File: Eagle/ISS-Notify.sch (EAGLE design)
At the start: 54 parts, among them J1 AVRISP, J2 JST2, J3 PROTOSPACE2, SW1 9077-1, SW2 SWITCH, U1 ATMEGA32U4, U2 MCP7940N, U3 TPS63001, U4 MCP73811, U5 TLC5971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

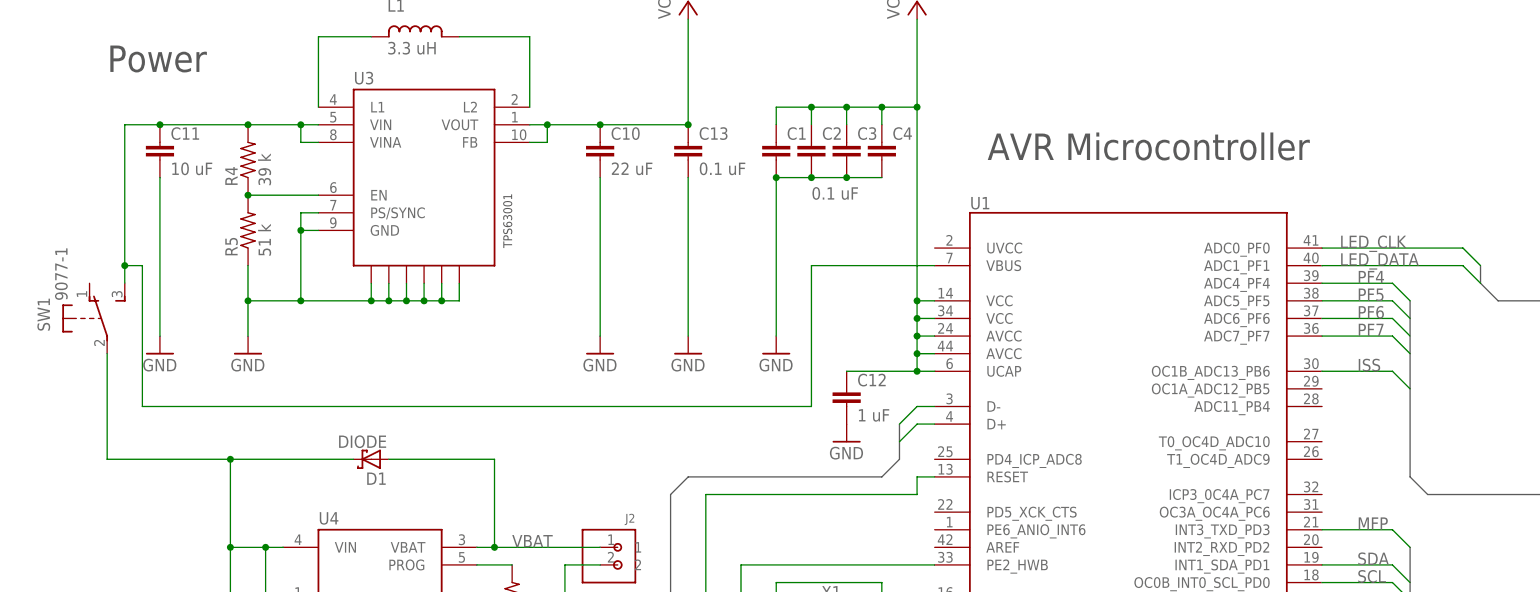
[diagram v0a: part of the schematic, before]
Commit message: bat sense signal
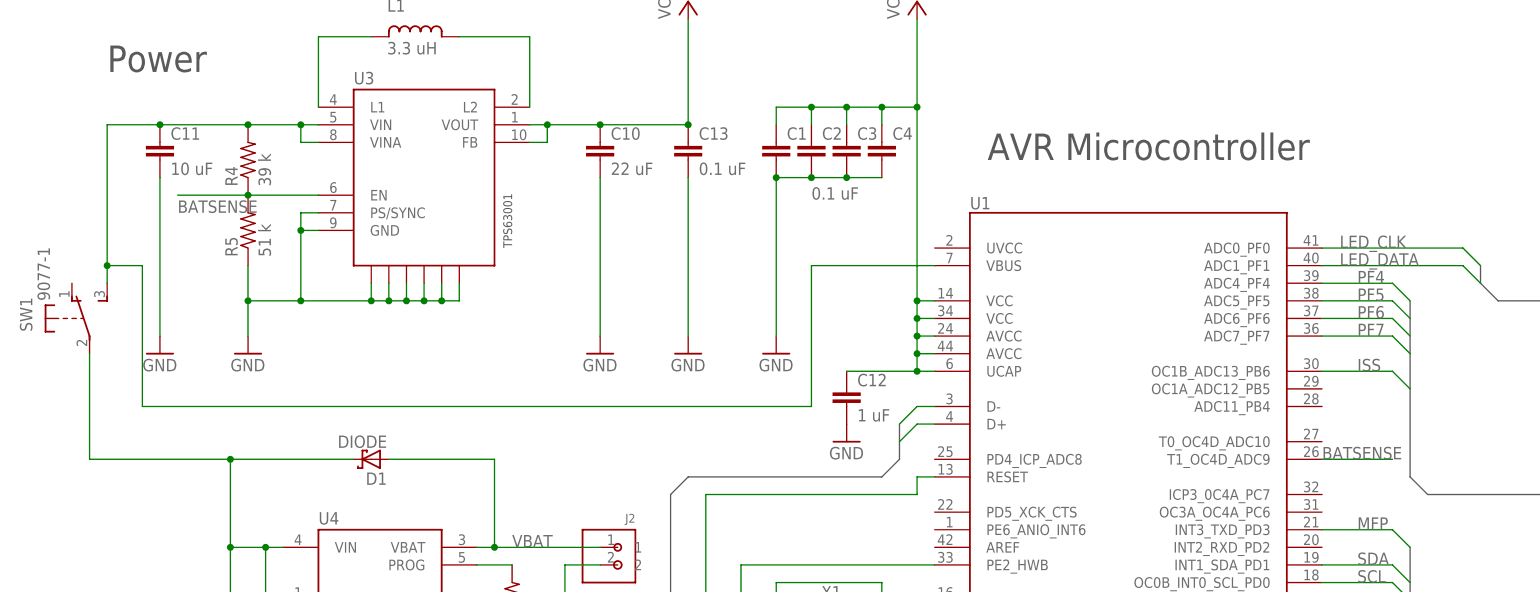
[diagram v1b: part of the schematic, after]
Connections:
- removed net N$3: R4.1, R5.2, U3.EN
- new net BATSENSE: R4.1, R5.2, U1.T1_OC4D_ADC9, U3.EN
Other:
- moved on the sheet: SW1
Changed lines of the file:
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@@
 <attribute name="VALUE" x="137.922" y="159.258" size="1.778" layer="96" rot="R180"/>
 </instance>
-<instance part="SW1" gate="1" x="30.48" y="205.74"/>
+<instance part="SW1" gate="1" x="27.94" y="205.74"/>
 <instance part="U4" gate="G$1" x="68.58" y="167.64"/>
 <instance part="R6" gate="R" x="88.9" y="165.1" rot="R90"/>
@@
 </segment>
 </net>
-<net name="N$3" class="0">
-<segment>
-<pinref part="R4" gate="R" pin="1"/>
-<pinref part="R5" gate="R" pin="2"/>
-<pinref part="U3" gate="G$1" pin="EN"/>
-<wire x1="60.96" y1="223.52" x2="50.8" y2="223.52" width="0.1524" layer="91"/>
-<junction x="50.8" y="223.52"/>
-</segment>
-</net>
 <net name="VIN" class="0">
 <segment>
@@
 <junction x="58.42" y="233.68"/>
 <pinref part="SW1" gate="1" pin="S"/>
-<wire x1="33.02" y1="210.82" x2="33.02" y2="213.36" width="0.1524" layer="91"/>
-<wire x1="33.02" y1="213.36" x2="33.02" y2="233.68" width="0.1524" layer="91"/>
-<wire x1="33.02" y1="233.68" x2="38.1" y2="233.68" width="0.1524" layer="91"/>
+<wire x1="30.48" y1="210.82" x2="30.48" y2="213.36" width="0.1524" layer="91"/>
+<wire x1="30.48" y1="213.36" x2="30.48" y2="233.68" width="0.1524" layer="91"/>
+<wire x1="30.48" y1="233.68" x2="38.1" y2="233.68" width="0.1524" layer="91"/>
 <junction x="38.1" y="233.68"/>
 <wire x1="132.08" y1="213.36" x2="132.08" y2="193.04" width="0.1524" layer="91"/>
 <wire x1="132.08" y1="193.04" x2="35.56" y2="193.04" width="0.1524" layer="91"/>
 <wire x1="35.56" y1="193.04" x2="35.56" y2="213.36" width="0.1524" layer="91"/>
-<wire x1="35.56" y1="213.36" x2="33.02" y2="213.36" width="0.1524" layer="91"/>
-<junction x="33.02" y="213.36"/>
+<wire x1="35.56" y1="213.36" x2="30.48" y2="213.36" width="0.1524" layer="91"/>
+<junction x="30.48" y="213.36"/>
 <pinref part="U1" gate="ATMEGA" pin="VBUS"/>
 <wire x1="149.86" y1="213.36" x2="132.08" y2="213.36" width="0.1524" layer="91"/>
@@
 <wire x1="66.04" y1="185.42" x2="48.26" y2="185.42" width="0.1524" layer="91"/>
 <pinref part="SW1" gate="1" pin="P"/>
-<wire x1="30.48" y1="200.66" x2="30.48" y2="185.42" width="0.1524" layer="91"/>
-<wire x1="30.48" y1="185.42" x2="48.26" y2="185.42" width="0.1524" layer="91"/>
+<wire x1="27.94" y1="200.66" x2="27.94" y2="185.42" width="0.1524" layer="91"/>
+<wire x1="27.94" y1="185.42" x2="48.26" y2="185.42" width="0.1524" layer="91"/>
 <junction x="48.26" y="185.42"/>
 </segment>
@@
 </segment>
 </net>
+<net name="BATSENSE" class="0">
+<segment>
+<pinref part="U1" gate="ATMEGA" pin="T1_OC4D_ADC9"/>
+<wire x1="205.74" y1="185.42" x2="215.9" y2="185.42" width="0.1524" layer="91"/>
+<label x="205.74" y="185.42" size="1.778" layer="95"/>
+</segment>
+<segment>
+<pinref part="R4" gate="R" pin="1"/>
+<pinref part="R5" gate="R" pin="2"/>
+<pinref part="U3" gate="G$1" pin="EN"/>
+<wire x1="60.96" y1="223.52" x2="50.8" y2="223.52" width="0.1524" layer="91"/>
+<junction x="50.8" y="223.52"/>
+<wire x1="50.8" y1="223.52" x2="40.64" y2="223.52" width="0.1524" layer="91"/>
+<label x="40.64" y="220.98" size="1.778" layer="95"/>
+</segment>
+</net>

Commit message: logo
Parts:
- added U$5: V0.3, ISS-Notify:LOGO
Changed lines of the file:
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@@
 <part name="U$4" library="ISS-Notify" deviceset="_4-BARE_MOUNTING_HOLE" device="/.300"/>
 <part name="C16" library="rcl_custom" deviceset="C-EU" device="0603-C-NOSILK" value="100 pF"/>
+<part name="U$5" library="ISS-Notify" deviceset="LOGO" device="" value="V0.3"/>
 </parts>
 <sheets>
@@
 <attribute name="VALUE" x="269.113" y="193.548" size="1.778" layer="96" rot="R90"/>
 </instance>
+<instance part="U$5" gate="G$1" x="22.86" y="22.86"/>
 </instances>
 <busses>

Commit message: Cut gerbers for OSH Park
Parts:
- renumbered J1 to AVRISP
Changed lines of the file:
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@@
 <parts>
 <part name="U1" library="ISS-Notify" deviceset="ATMEGA32U4" device=""/>
-<part name="J1" library="ISS-Notify" deviceset="AVRISP" device=""/>
+<part name="AVRISP" library="ISS-Notify" deviceset="AVRISP" device=""/>
 <part name="USB" library="ISS-Notify" deviceset="CON_USB-MICRO-6GND" device=""/>
 <part name="U2" library="ISS-Notify" deviceset="MCP7940N" device=""/>
@@
 <instances>
 <instance part="U1" gate="ATMEGA" x="177.8" y="177.8"/>
-<instance part="J1" gate="G$1" x="187.96" y="119.38"/>
+<instance part="AVRISP" gate="G$1" x="187.96" y="119.38"/>
 <instance part="USB" gate="CF" x="43.18" y="119.38" rot="MR270"/>
 <instance part="U2" gate="G$1" x="287.02" y="228.6"/>
@@
 </segment>
 <segment>
-<pinref part="J1" gate="G$1" pin="GND"/>
+<pinref part="AVRISP" gate="G$1" pin="GND"/>
 <wire x1="195.58" y1="114.3" x2="198.12" y2="114.3" width="0.1524" layer="91"/>
 <pinref part="GND16" gate="1" pin="GND"/>
@@
 </segment>
 <segment>
-<pinref part="J1" gate="G$1" pin="2"/>
+<pinref part="AVRISP" gate="G$1" pin="2"/>
 <wire x1="195.58" y1="124.46" x2="231.14" y2="124.46" width="0.1524" layer="91"/>
 <pinref part="P+4" gate="VCC" pin="VCC"/>
@@
 <net name="MISO" class="0">
 <segment>
-<pinref part="J1" gate="G$1" pin="1"/>
+<pinref part="AVRISP" gate="G$1" pin="1"/>
 <wire x1="195.58" y1="127" x2="210.82" y2="127" width="0.1524" layer="91"/>
 <wire x1="210.82" y1="127" x2="210.82" y2="160.02" width="0.1524" layer="91"/>
@@
 <net name="MOSI" class="0">
 <segment>
-<pinref part="J1" gate="G$1" pin="4"/>
+<pinref part="AVRISP" gate="G$1" pin="4"/>
 <wire x1="195.58" y1="119.38" x2="215.9" y2="119.38" width="0.1524" layer="91"/>
 <wire x1="215.9" y1="119.38" x2="215.9" y2="157.48" width="0.1524" layer="91"/>
@@
 <wire x1="205.74" y1="154.94" x2="213.36" y2="154.94" width="0.1524" layer="91"/>
 <wire x1="213.36" y1="154.94" x2="213.36" y2="121.92" width="0.1524" layer="91"/>
-<pinref part="J1" gate="G$1" pin="3"/>
+<pinref part="AVRISP" gate="G$1" pin="3"/>
 <wire x1="213.36" y1="121.92" x2="195.58" y2="121.92" width="0.1524" layer="91"/>
 <label x="198.12" y="121.92" size="1.778" layer="95"/>
@@
 <net name="RESET" class="0">
 <segment>
-<pinref part="J1" gate="G$1" pin="5"/>
+<pinref part="AVRISP" gate="G$1" pin="5"/>
 <wire x1="195.58" y1="116.84" x2="205.74" y2="116.84" width="0.1524" layer="91"/>
 <wire x1="205.74" y1="116.84" x2="205.74" y2="109.22" width="0.1524" layer="91"/>

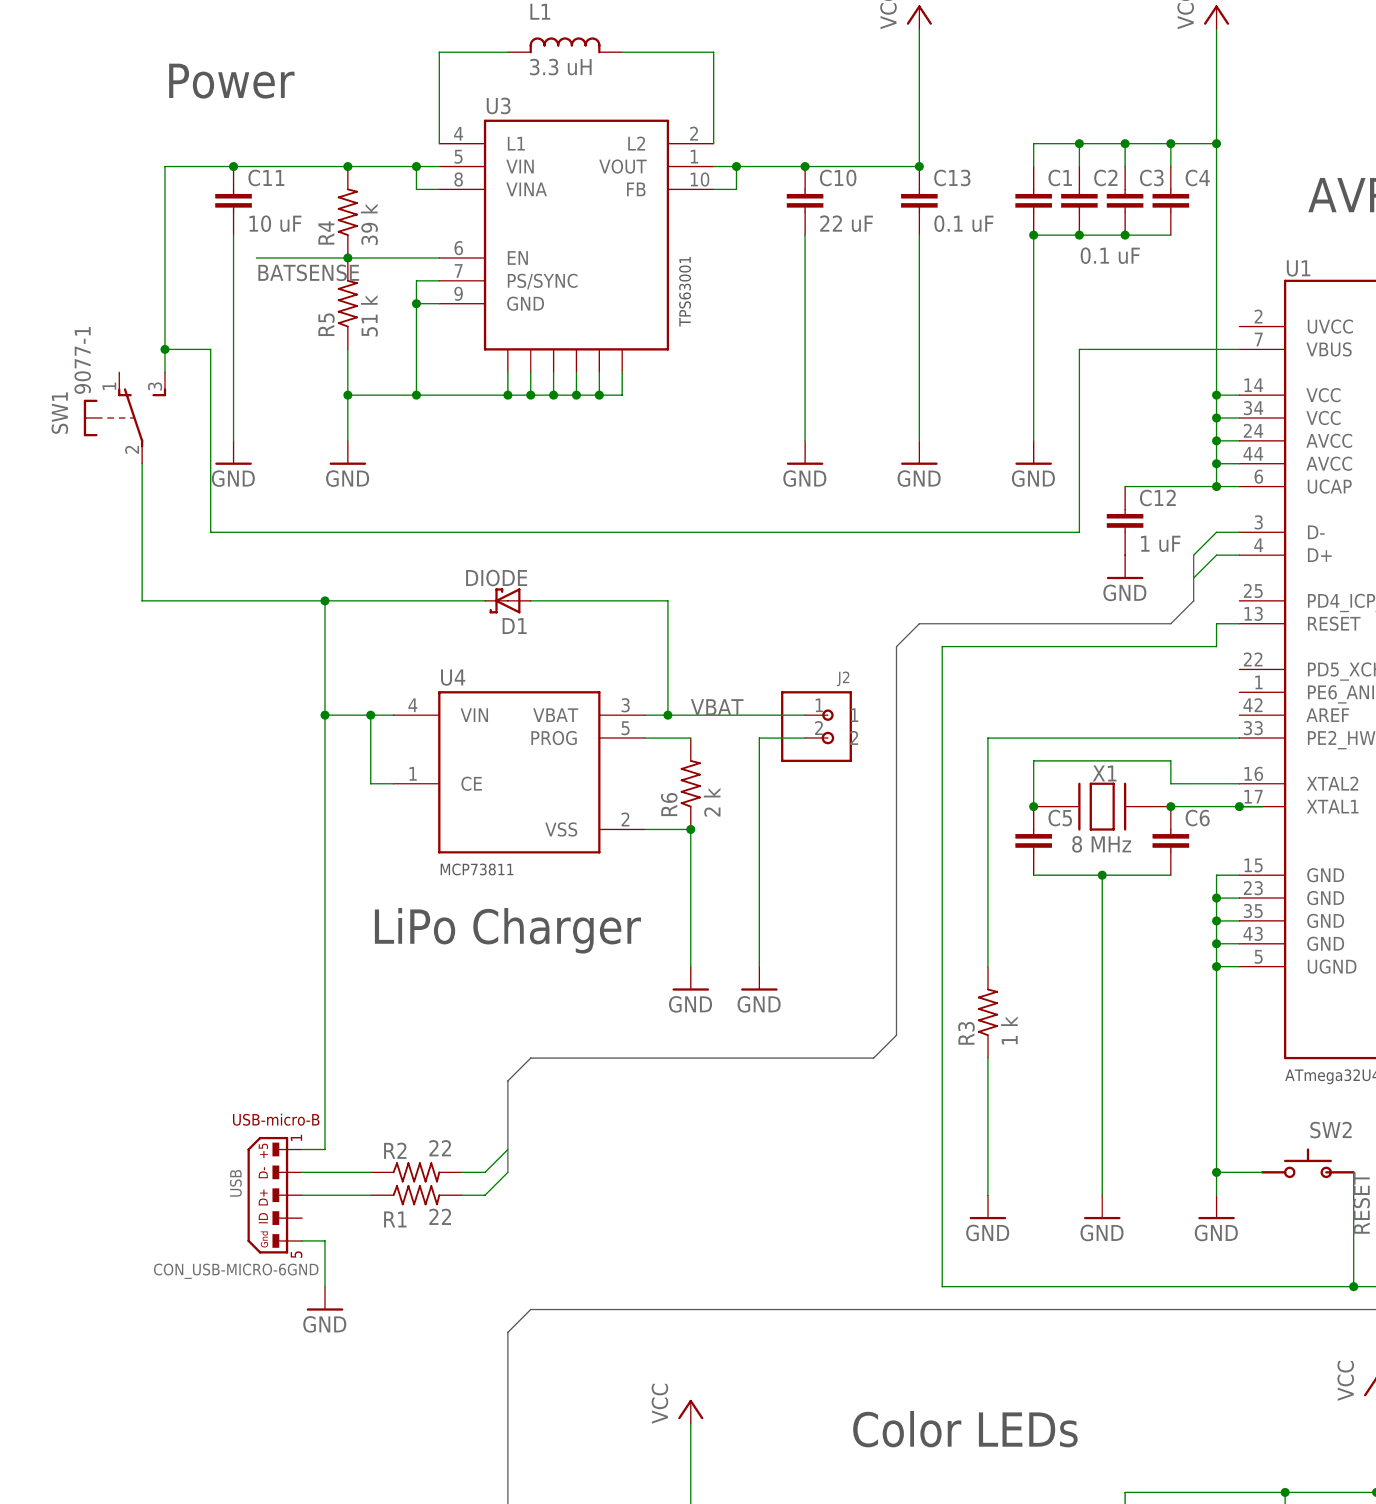
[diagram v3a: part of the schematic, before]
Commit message: Update parts after digikey searches
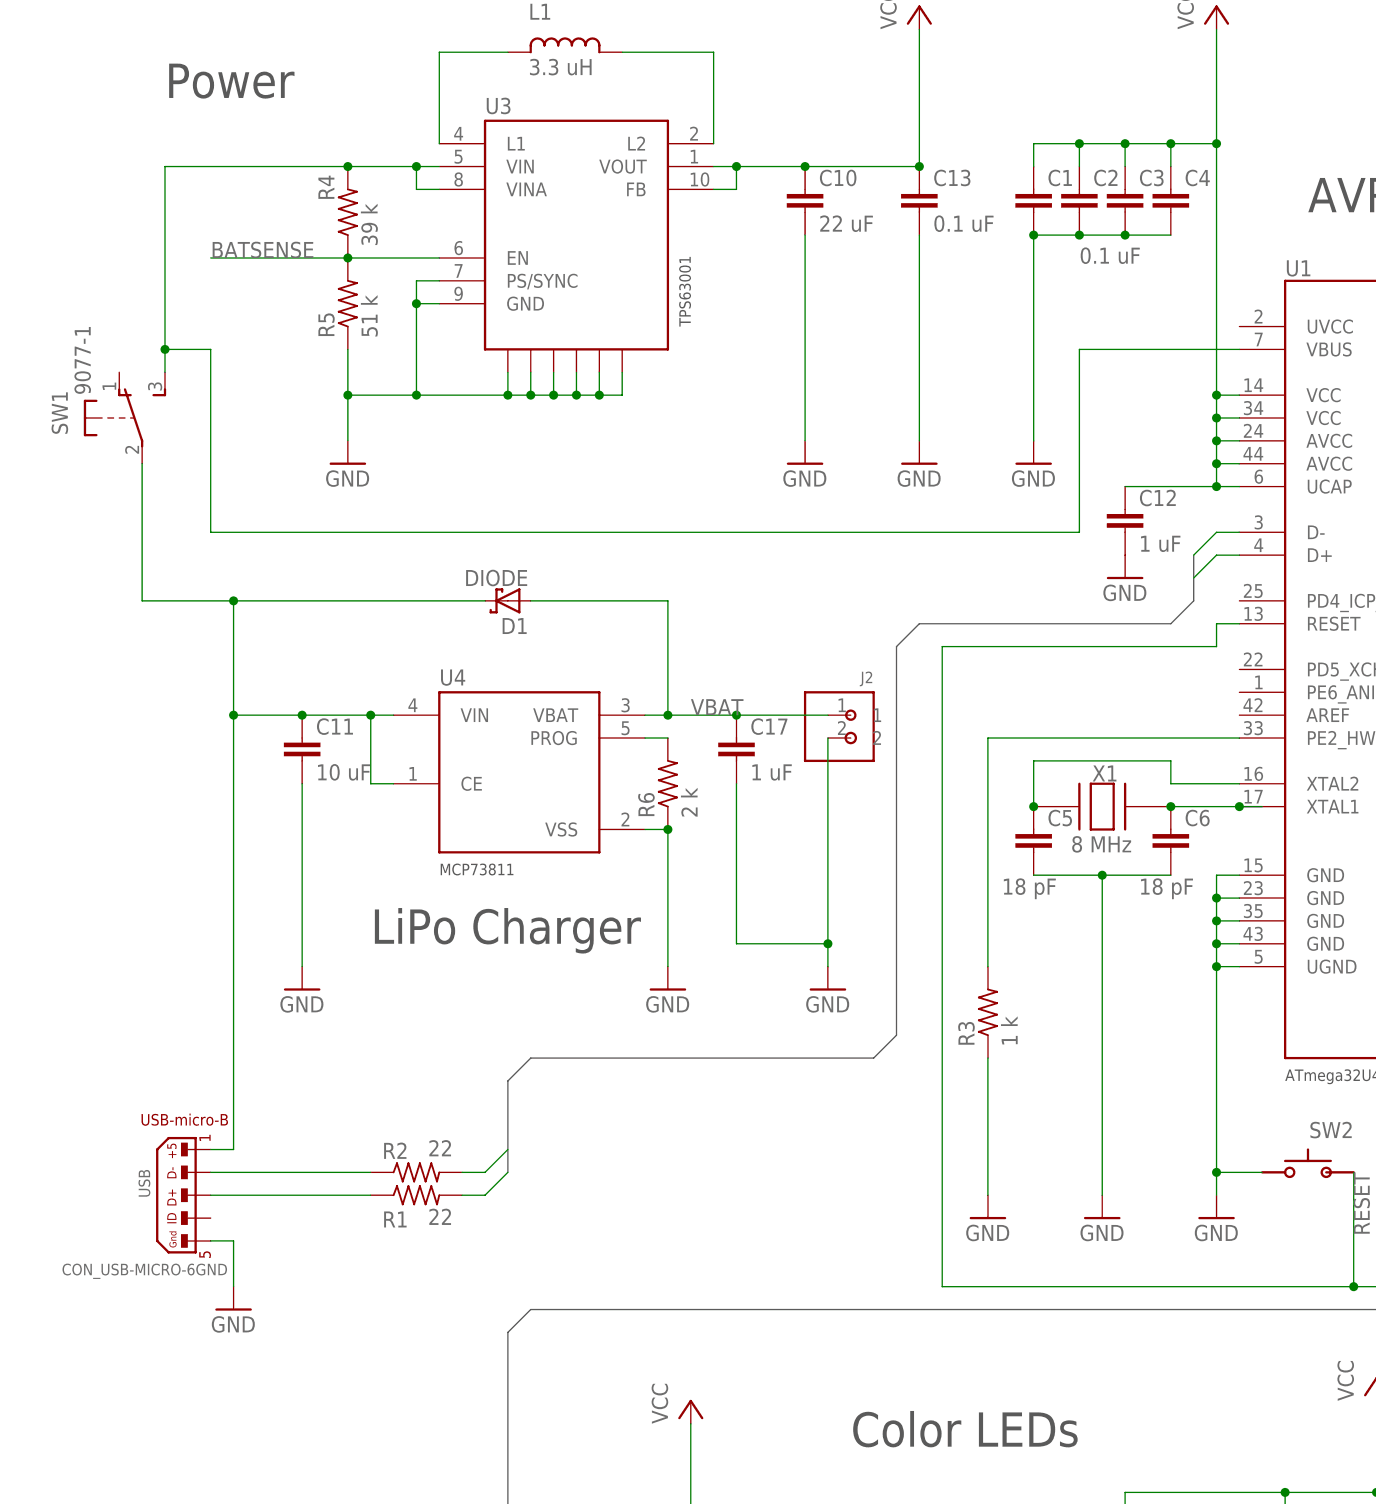
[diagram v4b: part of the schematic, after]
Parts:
- added C17: 1 uF, rcl_custom:C-EU0603-C-NOSILK
- C5, C6: value (none) -> 18 pF
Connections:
- net GND: now also C17.2
- net VBAT: now also C17.1
- net VIN: no longer C11.1
- net VUSB: now also C11.1
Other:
- moved on the sheet: C11, J2, R6, USB
